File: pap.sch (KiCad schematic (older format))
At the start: 0 parts

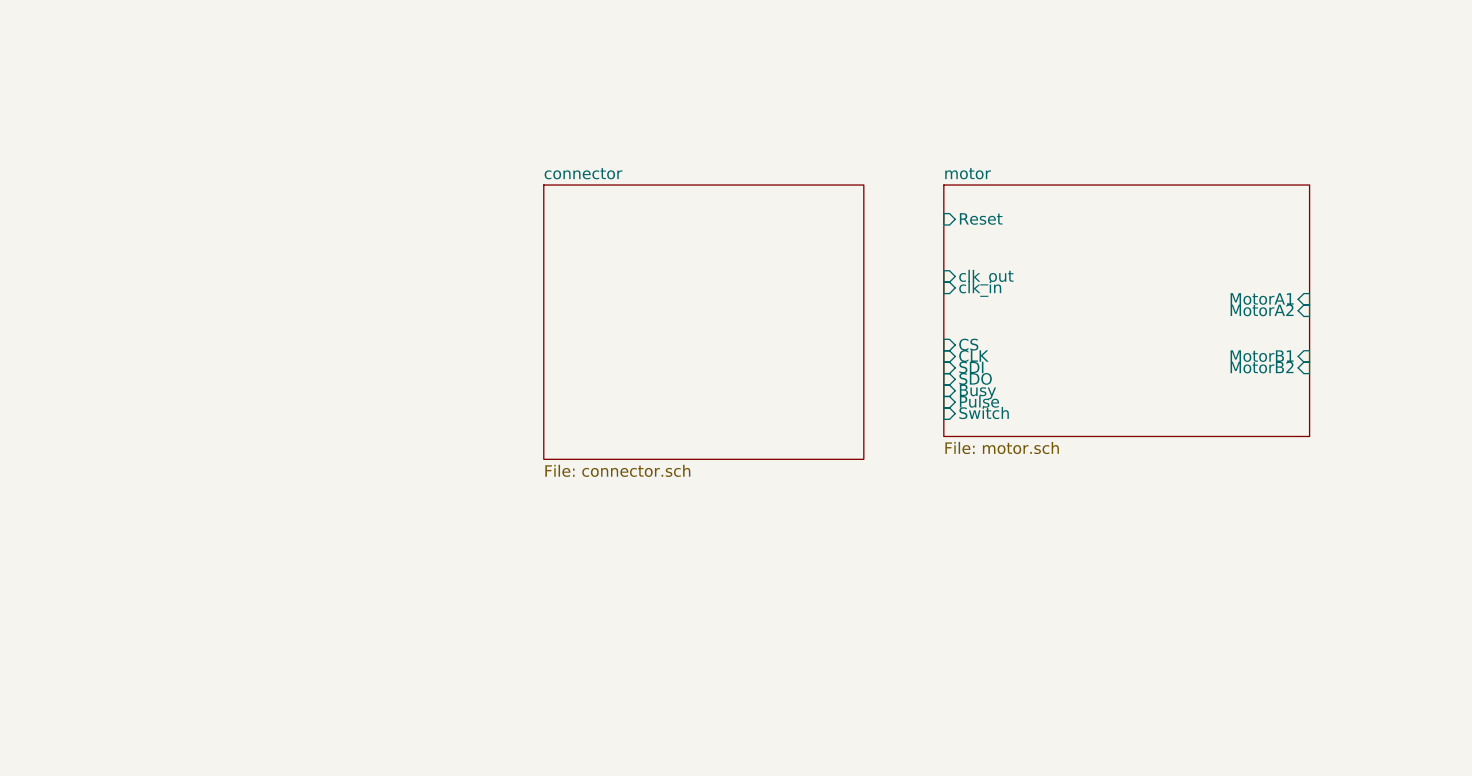
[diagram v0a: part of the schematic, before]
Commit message: agrego mas conectores y paso a pcb (todo mal!)
agregue conectores RJ45 para el encadenamiento spi y busyflag, pero no
para pulse.. es lo voy a mandar aparte porque es individual por cada
driver.. al igual que switch, y vere si alguna cosa mas.. en el rj me
sobran aun 2 pines.. ya vere que mando..lastima que no puedo mandar
pulse por ahi.. porque al ser 1 por driver necesito ir directo desde el
controlador.. sino como?... pase a pcb para ver que onda nada mas y
obvio me faltan definir los footprints de casi todo.. pero al menos
paso...orcad ya estaria llorando y no podria hacer nada...como sea, esta
bueno...sigo
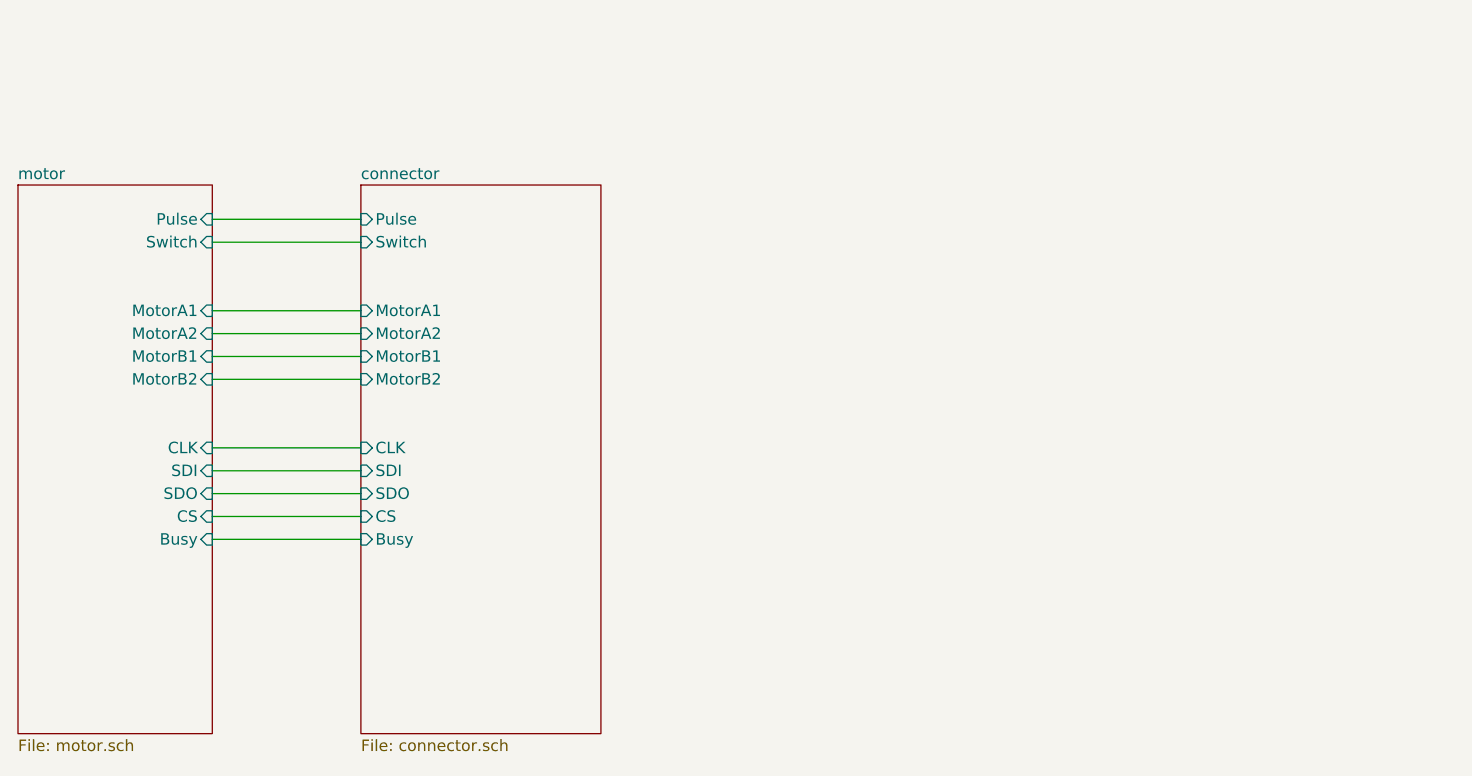
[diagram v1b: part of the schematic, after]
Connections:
- wire segments 0 -> 11
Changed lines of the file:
@@
 $EndDescr
 $Comp
-L schematic.lib:85V #PWR?
+L schematic.lib:85V #PWR0101
 U 1 1 5BA6D969
 P 15100 2450
-F 0 "#PWR?" H 15100 2350 50  0001 C CNN
+F 0 "#PWR0101" H 15100 2350 50  0001 C CNN
 F 1 "85V" H 15100 2725 50  0000 C CNN
 F 2 "" H 15100 2450 50  0001 C CNN
@@
 $EndComp
 $Comp
-L schematic.lib:G85V #PWR?
+L schematic.lib:G85V #PWR0102
 U 1 1 5BA6D9CB
 P 15100 2650
-F 0 "#PWR?" H 15100 2400 50  0001 C CNN
+F 0 "#PWR0102" H 15100 2400 50  0001 C CNN
 F 1 "G85V" H 15105 2477 50  0000 C CNN
 F 2 "" H 15100 2650 50  0001 C CNN
@@
 $EndComp
 $Comp
-L schematic.lib:15V #PWR?
+L schematic.lib:15V #PWR0103
 U 1 1 5BA6DA3B
 P 14850 2450
-F 0 "#PWR?" H 14850 2350 50  0001 C CNN
+F 0 "#PWR0103" H 14850 2350 50  0001 C CNN
 F 1 "15V" H 14850 2725 50  0000 C CNN
 F 2 "" H 14850 2450 50  0001 C CNN
@@
 $EndComp
 $Comp
-L schematic.lib:G15V #PWR?
+L schematic.lib:G15V #PWR0104
 U 1 1 5BA6DA9D
 P 14850 2650
-F 0 "#PWR?" H 14850 2400 50  0001 C CNN
+F 0 "#PWR0104" H 14850 2400 50  0001 C CNN
 F 1 "G15V" H 14855 2477 50  0000 C CNN
 F 2 "" H 14850 2650 50  0001 C CNN
@@
 $EndComp
 $Comp
-L schematic.lib:100V #PWR?
+L schematic.lib:100V #PWR0105
 U 1 1 5BA6DB22
 P 15350 2450
-F 0 "#PWR?" H 15350 2350 50  0001 C CNN
+F 0 "#PWR0105" H 15350 2350 50  0001 C CNN
 F 1 "100V" H 15350 2725 50  0000 C CNN
 F 2 "" H 15350 2450 50  0001 C CNN
@@
 $EndComp
 $Comp
-L schematic.lib:3V3 #PWR?
+L schematic.lib:3V3 #PWR0106
 U 1 1 5BA6DB92
 P 14600 2450
-F 0 "#PWR?" H 14600 2350 50  0001 C CNN
+F 0 "#PWR0106" H 14600 2350 50  0001 C CNN
 F 1 "3V3" H 14600 2725 50  0000 C CNN
 F 2 "" H 14600 2450 50  0001 C CNN
@@
 $EndComp
 $Comp
-L schematic.lib:G3V3 #PWR?
+L schematic.lib:G3V3 #PWR0107
 U 1 1 5BA6DC0E
 P 14600 2650
-F 0 "#PWR?" H 14600 2400 50  0001 C CNN
+F 0 "#PWR0107" H 14600 2400 50  0001 C CNN
 F 1 "G3V3" H 14605 2477 50  0000 C CNN
 F 2 "" H 14600 2650 50  0001 C CNN
@@
 $EndComp
 $Sheet
-S 6000 3650 1400 1200
+S 3700 3650 850  2400
+U 5BA6E8FB
+F0 "motor" 50
+F1 "motor.sch" 50
+F2 "MotorA1" I R 4550 4200 50
+F3 "MotorA2" I R 4550 4300 50
+F4 "MotorB1" I R 4550 4400 50
+F5 "MotorB2" I R 4550 4500 50
+F8 "CS" I R 4550 5100 50
+F9 "CLK" I R 4550 4800 50
+F10 "SDI" I R 4550 4900 50
+F11 "SDO" I R 4550 5000 50
+F12 "Busy" I R 4550 5200 50
+F13 "Pulse" I R 4550 3800 50
+F14 "Switch" I R 4550 3900 50
+$EndSheet
+$Sheet
+S 5200 3650 1050 2400
 U 5BA6E5CE
 F0 "connector" 50
 F1 "connector.sch" 50
+F2 "CS" I L 5200 5100 50
+F3 "CLK" I L 5200 4800 50
+F4 "SDI" I L 5200 4900 50
+F5 "Busy" I L 5200 5200 50
+F6 "Pulse" I L 5200 3800 50
+F7 "Switch" I L 5200 3900 50
+F8 "MotorB2" I L 5200 4500 50
+F9 "MotorA2" I L 5200 4300 50
+F10 "MotorA1" I L 5200 4200 50
+F11 "MotorB1" I L 5200 4400 50
+F12 "SDO" I L 5200 5000 50
 $EndSheet
-$Sheet
-S 7750 3650 1600 1100
-U 5BA6E8FB
-F0 "motor" 50
-F1 "motor.sch" 50
-F2 "MotorA1" I R 9350 4150 50
-F3 "MotorA2" I R 9350 4200 50
-F4 "MotorB1" I R 9350 4400 50
-F5 "MotorB2" I R 9350 4450 50
-F6 "clk_out" I L 7750 4050 50
-F7 "clk_in" I L 7750 4100 50
-F8 "CS" I L 7750 4350 50
-F9 "CLK" I L 7750 4400 50
-F10 "SDI" I L 7750 4450 50
-F11 "SDO" I L 7750 4500 50
-F12 "Busy" I L 7750 4550 50
-F13 "Pulse" I L 7750 4600 50
-F14 "Switch" I L 7750 4650 50
-F15 "Reset" I L 7750 3800 50
-$EndSheet
+Wire Wire Line
+	5200 3800 4550 3800
+Wire Wire Line
+	4550 3900 5200 3900
+Wire Wire Line
+	5200 4200 4550 4200
+Wire Wire Line
+	5200 4300 4550 4300
+Wire Wire Line
+	5200 4400 4550 4400
+Wire Wire Line
+	4550 4500 5200 4500
+Wire Wire Line
+	4550 4900 5200 4900
+Wire Wire Line
+	4550 4800 5200 4800
+Wire Wire Line
+	4550 5000 5200 5000
+Wire Wire Line
+	5200 5100 4550 5100
+Wire Wire Line
+	4550 5200 5200 5200
 $EndSCHEMATC

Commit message: armo huella step01 y asigno casi todas las huellas
ahi hice el landpattern del steo01, que es un parto, pero quedo bueno..
al tiempo que aprendi a editar y la verdad es que es comodo.. me animo a
decir que supera a allegro, y de hecho se parece demasiado en muchas
cosas.. huele a copia de algun lado.. incluiso los nombres en los menus
son iguales... como sea, ya quedo eso, lo que si tuve que volar algunos
pines repetidos en el simbolo porque sino era un chino tener muchos
pines repetidos, o sea en la huella tengo un pin que va a parar a
multiples pines en el esquemativo. si bien lo logre hacer superponiendo
encimados los pines en el esquemativo y dejandolos invisibles excepto
uno, eso funca, pero es un azco... preferi volar todos y dejar la union
univoca y listo.. al simbolo le faltan pines, pero el landpattern no los
necesita porque se unen todos en una misma masa de pad. despues pase
todas las huellas del resto del chiquitaje y ademas acomodo los power
netlist que estaban mal y de paso voy puliendo el disenio en general..
va quedando.. un poco mas y paso a tirar pista
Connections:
- net labels removed: 100V, 15V, 3V3, 85V, G15V, G3V3, G85V
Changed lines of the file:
@@
 Comment4 ""
 $EndDescr
-$Comp
-L schematic.lib:85V #PWR0101
-U 1 1 5BA6D969
-P 15100 2450
-F 0 "#PWR0101" H 15100 2350 50  0001 C CNN
-F 1 "85V" H 15100 2725 50  0000 C CNN
-F 2 "" H 15100 2450 50  0001 C CNN
-F 3 "" H 15100 2450 50  0001 C CNN
-	1    15100 2450
-	1    0    0    -1
-$EndComp
-$Comp
-L schematic.lib:G85V #PWR0102
-U 1 1 5BA6D9CB
-P 15100 2650
-F 0 "#PWR0102" H 15100 2400 50  0001 C CNN
-F 1 "G85V" H 15105 2477 50  0000 C CNN
-F 2 "" H 15100 2650 50  0001 C CNN
-F 3 "" H 15100 2650 50  0001 C CNN
-	1    15100 2650
-	1    0    0    -1
-$EndComp
-$Comp
-L schematic.lib:15V #PWR0103
-U 1 1 5BA6DA3B
-P 14850 2450
-F 0 "#PWR0103" H 14850 2350 50  0001 C CNN
-F 1 "15V" H 14850 2725 50  0000 C CNN
-F 2 "" H 14850 2450 50  0001 C CNN
-F 3 "" H 14850 2450 50  0001 C CNN
-	1    14850 2450
-	1    0    0    -1
-$EndComp
-$Comp
-L schematic.lib:G15V #PWR0104
-U 1 1 5BA6DA9D
-P 14850 2650
-F 0 "#PWR0104" H 14850 2400 50  0001 C CNN
-F 1 "G15V" H 14855 2477 50  0000 C CNN
-F 2 "" H 14850 2650 50  0001 C CNN
-F 3 "" H 14850 2650 50  0001 C CNN
-	1    14850 2650
-	1    0    0    -1
-$EndComp
-$Comp
-L schematic.lib:100V #PWR0105
-U 1 1 5BA6DB22
-P 15350 2450
-F 0 "#PWR0105" H 15350 2350 50  0001 C CNN
-F 1 "100V" H 15350 2725 50  0000 C CNN
-F 2 "" H 15350 2450 50  0001 C CNN
-F 3 "" H 15350 2450 50  0001 C CNN
-	1    15350 2450
-	1    0    0    -1
-$EndComp
-$Comp
-L schematic.lib:3V3 #PWR0106
-U 1 1 5BA6DB92
-P 14600 2450
-F 0 "#PWR0106" H 14600 2350 50  0001 C CNN
-F 1 "3V3" H 14600 2725 50  0000 C CNN
-F 2 "" H 14600 2450 50  0001 C CNN
-F 3 "" H 14600 2450 50  0001 C CNN
-	1    14600 2450
-	1    0    0    -1
-$EndComp
-$Comp
-L schematic.lib:G3V3 #PWR0107
-U 1 1 5BA6DC0E
-P 14600 2650
-F 0 "#PWR0107" H 14600 2400 50  0001 C CNN
-F 1 "G3V3" H 14605 2477 50  0000 C CNN
-F 2 "" H 14600 2650 50  0001 C CNN
-F 3 "" H 14600 2650 50  0001 C CNN
-	1    14600 2650
-	1    0    0    -1
-$EndComp
-$Sheet
-S 3700 3650 850  2400
-U 5BA6E8FB
-F0 "motor" 50
-F1 "motor.sch" 50
-F2 "MotorA1" I R 4550 4200 50
-F3 "MotorA2" I R 4550 4300 50
-F4 "MotorB1" I R 4550 4400 50
-F5 "MotorB2" I R 4550 4500 50
-F8 "CS" I R 4550 5100 50
-F9 "CLK" I R 4550 4800 50
-F10 "SDI" I R 4550 4900 50
-F11 "SDO" I R 4550 5000 50
-F12 "Busy" I R 4550 5200 50
-F13 "Pulse" I R 4550 3800 50
-F14 "Switch" I R 4550 3900 50
-$EndSheet
 $Sheet
 S 5200 3650 1050 2400
@@
 Wire Wire Line
 	4550 5200 5200 5200
+$Sheet
+S 3700 3650 850  2400
+U 5BA6E8FB
+F0 "motor" 50
+F1 "motor.sch" 50
+F2 "MotorA1" I R 4550 4200 50
+F3 "MotorA2" I R 4550 4300 50
+F4 "MotorB1" I R 4550 4400 50
+F5 "MotorB2" I R 4550 4500 50
+F6 "CS" I R 4550 5100 50
+F7 "CLK" I R 4550 4800 50
+F8 "SDI" I R 4550 4900 50
+F9 "SDO" I R 4550 5000 50
+F10 "Busy" I R 4550 5200 50
+F11 "Pulse" I R 4550 3800 50
+F12 "Switch" I R 4550 3900 50
+$EndSheet
 $EndSCHEMATC

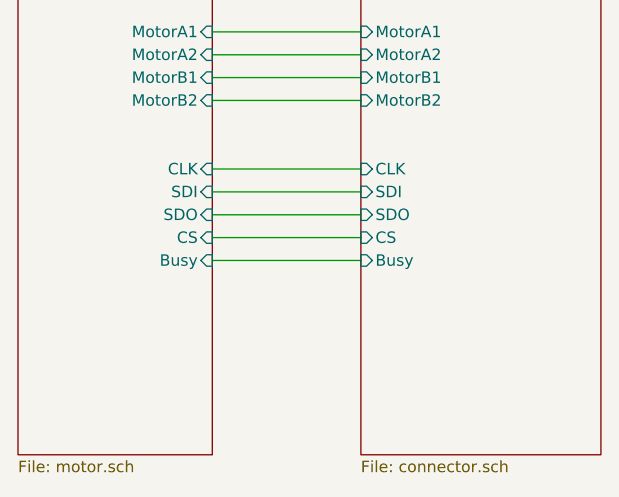
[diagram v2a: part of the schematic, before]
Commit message: arranco a rutear, cambio xtal por SMD y opcion CLKIN
arranque a tirar pist porque me estaba aburriendo ya, de paso voy
practivcando los shortcuts y demas.. esta muy copado y te aviso.. es
plagio a allegro.. no cabe dudas.. como sea, cambie el Xtal por uno SMD
de 4 pines que se consigue y minimiza el espacio, agegue tambien clkin
para mandar clk a todos por igual con el PWM del uC para sincronizar con
un selector para poder usar el xtal si es que el PWM se pierde por
fanout o ruido.. y no mucho mas
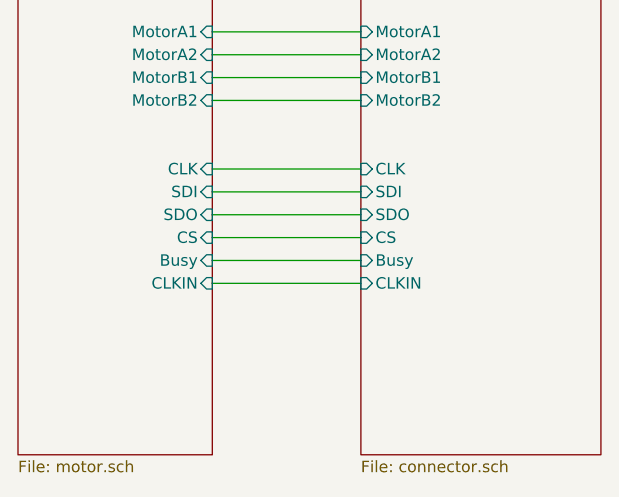
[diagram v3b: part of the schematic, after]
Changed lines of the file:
@@
 F11 "MotorB1" I L 5200 4400 50
 F12 "SDO" I L 5200 5000 50
+F13 "CLKIN" I L 5200 5300 50
 $EndSheet
 Wire Wire Line
@@
 F11 "Pulse" I R 4550 3800 50
 F12 "Switch" I R 4550 3900 50
+F13 "CLKIN" I R 4550 5300 50
 $EndSheet
+Wire Wire Line
+	4550 5300 5200 5300
 $EndSCHEMATC
